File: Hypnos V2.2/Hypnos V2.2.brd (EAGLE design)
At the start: 25.6 x 52 mm, 32 parts

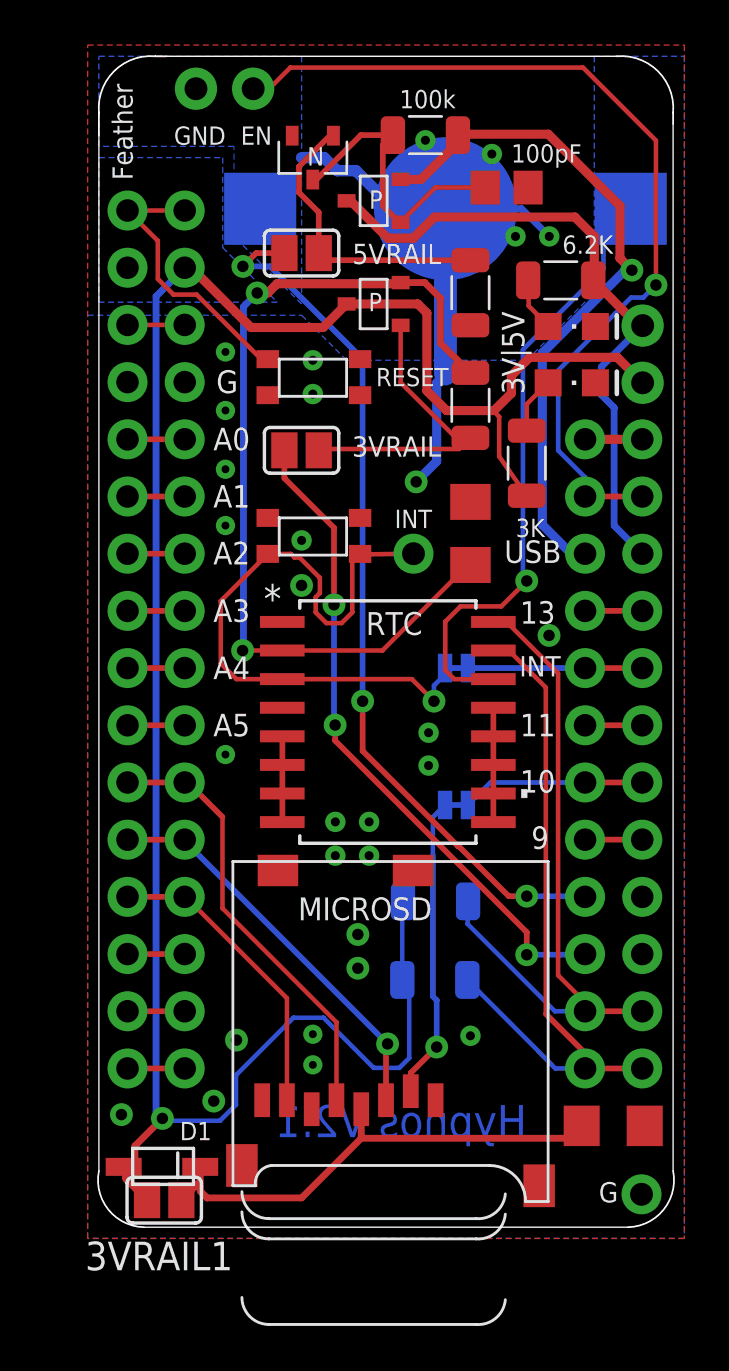
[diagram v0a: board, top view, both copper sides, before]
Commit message: Hypnos 2.2 and 3.2
+Change solder bridge to always connected pad
+Remove solder bridge for D1 diode
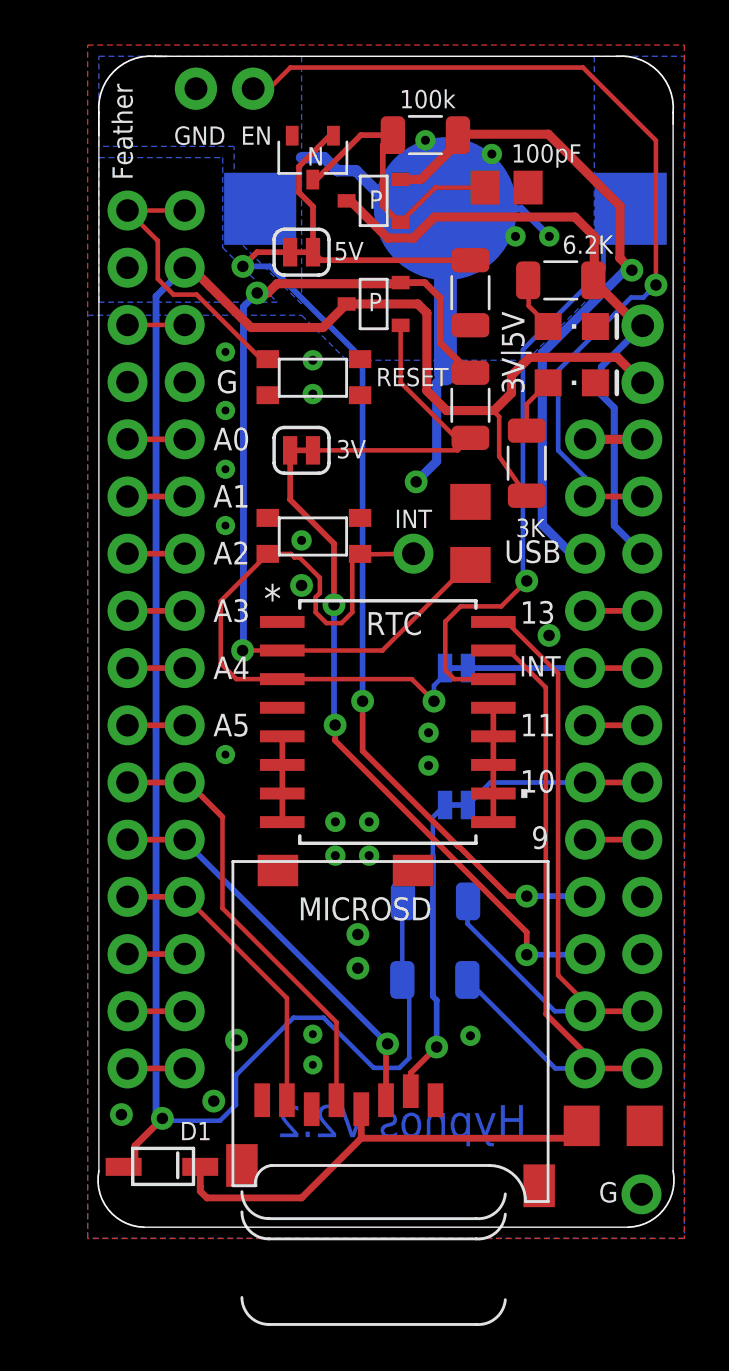
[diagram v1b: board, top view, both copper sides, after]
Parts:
- removed 3VRAIL, 3VRAIL1, 5VRAIL: (no value), jumper:SJ
- added 3V, 5V: (no value), SparkFun-Jumpers:SMT-JUMPER_2_NC_TRACE_SILK
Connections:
- removed net N$5: 3VRAIL.2, PMOS2.G, R2.1
- new net 5V: 3V.2, PMOS2.G, R2.1
- net 3VRAIL: no longer 3VRAIL1.2
- net N$1: now also 5V.1; no longer 5VRAIL.1
- net N$3: now also 3V.1; no longer 3VRAIL.1
- net N$4: now also 5V.2; no longer 5VRAIL.2
- net VDD: no longer 3VRAIL1.1
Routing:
- net 5V: track 0.00 -> 14.0 mm
- net N$5: track 13.8 -> 0.00 mm
- net 3VRAIL: track 97.2 -> 95.3 mm
- net VDD: track 22.0 -> 20.8 mm
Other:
- board text added: "Hypnos V2.2"
- board text removed: "Hypnos V2.1"
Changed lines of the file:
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@@
 <layer number="21" name="tPlace" color="7" fill="1" visible="yes" active="yes"/>
 <layer number="22" name="bPlace" color="7" fill="1" visible="yes" active="yes"/>
-<layer number="23" name="tOrigins" color="15" fill="1" visible="no" active="yes"/>
+<layer number="23" name="tOrigins" color="15" fill="1" visible="yes" active="yes"/>
 <layer number="24" name="bOrigins" color="15" fill="1" visible="yes" active="yes"/>
 <layer number="25" name="tNames" color="7" fill="1" visible="yes" active="yes"/>
@@
 <text x="12.18" y="17.66" size="1.016" layer="22" rot="MR270">Optional
 I2C Pull Up</text>
-<text x="20" y="4.5" size="1.4224" layer="16" ratio="15" rot="MR0">Hypnos V2.1</text>
+<text x="20" y="4.5" size="1.4224" layer="16" ratio="15" rot="MR0">Hypnos V2.2</text>
 <text x="18.2" y="2.9" size="1.016" layer="22" rot="MR0">OpenSlab</text>
 <text x="11.79" y="19.71" size="1.016" layer="22" ratio="10" rot="MR180">SDCS</text>
@@
 <text x="19.51" y="31.15" size="0.8128" layer="21">3K</text>
 <text x="23.2" y="1.6" size="0.9" layer="21" ratio="10">G</text>
-<text x="22.9" y="1.3" size="1.016" layer="22" rot="MR0">Bao Nguyen &amp; Bryson Goto</text>
+<text x="23.7" y="1.2" size="1.016" layer="22" rot="MR0">Bao Nguyen &amp; Bryson Goto</text>
 <wire x1="26.5" y1="50" x2="26.5" y2="49.5" width="0.0762" layer="20"/>
 <wire x1="1" y1="49" x2="1" y2="50" width="0.0762" layer="20"/>
@@
 <wire x1="2.5" y1="2.4" x2="2.5" y2="4" width="0.15" layer="21"/>
 <wire x1="4.5" y1="3.8" x2="4.5" y2="2.7" width="0.15" layer="21"/>
-<text x="20" y="4.5" size="1.4224" layer="30" ratio="15" rot="MR0">Hypnos V2.1</text>
+<text x="20" y="4.5" size="1.4224" layer="30" ratio="15" rot="MR0">Hypnos V2.2</text>
 </plain>
 <attributes>
@@
 <attribute name="VENDOR" value="Maxim Integrated Products" x="69.712" y="-7.546" size="1.778" layer="27" display="off"/>
 </element>
-<element name="5VRAIL" library="jumper" library_urn="urn:adsk.eagle:library:252" package="SJ" package3d_urn="urn:adsk.eagle:package:15471/1" value="" x="10" y="43.76" smashed="yes">
-<attribute name="NAME" x="12.259" y="43.273" size="0.9" layer="25" ratio="10"/>
-<attribute name="VALUE" x="10.4001" y="43.76" size="0.02" layer="27"/>
-</element>
-<element name="3VRAIL" library="jumper" library_urn="urn:adsk.eagle:library:252" package="SJ" package3d_urn="urn:adsk.eagle:package:15471/1" value="" x="10" y="35" smashed="yes">
-<attribute name="NAME" x="12.246" y="34.719" size="0.9" layer="25" ratio="10"/>
-<attribute name="VALUE" x="10.4001" y="35" size="0.02" layer="27"/>
-</element>
 <element name="R2" library="Resistor_Capacitor" library_urn="urn:adsk.eagle:library:11396451" package="RES_1206" package3d_urn="urn:adsk.eagle:package:10872898/2" value="30k" x="17.5" y="37" smashed="yes" rot="R90">
 <attribute name="CREATED_BY" value="PCBLayout.com" x="17.5" y="37" size="1.778" layer="27" rot="R90" display="off"/>
@@
 <attribute name="VALUE" x="5.705" y="6.355" size="1.27" layer="27" rot="R180"/>
 </element>
-<element name="3VRAIL1" library="jumper" library_urn="urn:adsk.eagle:library:252" package="SJ" package3d_urn="urn:adsk.eagle:package:15471/1" value="" x="3.9" y="1.7" smashed="yes" rot="R180">
-<attribute name="NAME" x="6.951" y="-0.143" size="1.27" layer="25" ratio="10" rot="R180"/>
-<attribute name="VALUE" x="3.4999" y="1.7" size="0.02" layer="27" rot="R180"/>
+<element name="5V" library="SparkFun-Jumpers" library_urn="urn:adsk.eagle:library:528" package="SMT-JUMPER_2_NC_TRACE_SILK" package3d_urn="urn:adsk.eagle:package:39281/1" value="" x="10" y="43.8" smashed="yes">
+<attribute name="NAME" x="12.1" y="43.443" size="0.8128" layer="25" font="vector" ratio="10" align="bottom-center"/>
+<attribute name="VALUE" x="10" y="42.657" size="0.6096" layer="27" font="vector" ratio="20" align="top-center"/>
+</element>
+<element name="3V" library="SparkFun-Jumpers" library_urn="urn:adsk.eagle:library:528" package="SMT-JUMPER_2_NC_TRACE_SILK" package3d_urn="urn:adsk.eagle:package:39281/1" value="" x="10" y="35" smashed="yes">
+<attribute name="NAME" x="12.2" y="34.643" size="0.8128" layer="25" font="vector" ratio="10" align="bottom-center"/>
+<attribute name="VALUE" x="10" y="33.857" size="0.6096" layer="27" font="vector" ratio="20" align="top-center"/>
 </element>
 </elements>
@@
 </signal>
 <signal name="N$1">
-<contactref element="5VRAIL" pad="1"/>
 <via x="7.3927125" y="43.1692" extent="1-16" drill="0.508"/>
 <wire x1="12.71" y1="39.0619125" x2="8.602646875" y2="43.169265625" width="0.254" layer="16"/>
@@
 <wire x1="12.71" y1="21.653025" x2="16.950925" y2="17.4121" width="0.254" layer="1"/>
 <wire x1="12.71" y1="23.86" x2="12.71" y2="21.653025" width="0.254" layer="1"/>
-<wire x1="9.238" y1="43.76" x2="7.9835125" y2="43.76" width="0.254" layer="1"/>
-<wire x1="7.3927125" y1="43.1692" x2="7.9835125" y2="43.76" width="0.254" layer="1"/>
 <contactref element="MS2" pad="20"/>
 <wire x1="20" y1="15.2" x2="22.56" y2="15.2" width="0.254" layer="16"/>
 <wire x1="22.56" y1="15.2" x2="22.59" y2="15.17" width="0.254" layer="16"/>
+<contactref element="5V" pad="1"/>
+<wire x1="9.492" y1="43.8" x2="8.0235125" y2="43.8" width="0.254" layer="1"/>
+<wire x1="8.0235125" y1="43.8" x2="7.3927125" y2="43.1692" width="0.254" layer="1"/>
 </signal>
 <signal name="N$3">
-<contactref element="3VRAIL" pad="1"/>
-<wire x1="11.44" y1="31.56" x2="9.238" y2="33.762" width="0.254" layer="1"/>
-<wire x1="9.238" y1="35" x2="9.238" y2="33.762" width="0.254" layer="1"/>
-<wire x1="11.44" y1="31.56" x2="11.44" y2="28.14" width="0.254" layer="1"/>
+<wire x1="11.44" y1="30.86" x2="11.44" y2="28.14" width="0.254" layer="1"/>
 <via x="11.44" y="28.14" extent="1-16" drill="0.508"/>
 <wire x1="11.44" y1="28.14" x2="11.44" y2="22.85" width="0.254" layer="16"/>
@@
 <wire x1="20" y1="12.6" x2="22.56" y2="12.6" width="0.254" layer="16"/>
 <wire x1="22.56" y1="12.6" x2="22.59" y2="12.63" width="0.254" layer="16"/>
+<contactref element="3V" pad="1"/>
+<wire x1="9.492" y1="35" x2="9.492" y2="32.808" width="0.254" layer="1"/>
+<wire x1="9.492" y1="32.808" x2="11.44" y2="30.86" width="0.254" layer="1"/>
 </signal>
 <signal name="5VUSB">
@@
 <wire x1="2.6" y1="3.4" x2="2.5" y2="3.3" width="0.3048" layer="1"/>
 <wire x1="2.5" y1="3.3" x2="2.1" y2="3.18" width="0.3048" layer="1"/>
-<contactref element="3VRAIL1" pad="2"/>
-<wire x1="3.138" y1="1.7" x2="2.2" y2="2.638" width="0.3048" layer="1"/>
-<wire x1="2.2" y1="2.638" x2="2.1" y2="3.18" width="0.3048" layer="1"/>
 <contactref element="R7" pad="1"/>
 <contactref element="R6" pad="1"/>
@@
 <wire x1="10.657625" y1="47.0255" x2="12.632125" y2="49" width="0.254" layer="1"/>
 </signal>
-<signal name="N$5">
-<contactref element="3VRAIL" pad="2"/>
+<signal name="5V">
 <contactref element="R2" pad="1"/>
 <contactref element="PMOS2" pad="G"/>
@@
 <wire x1="17.121728125" y1="35.288271875" x2="14.4" y2="38.01" width="0.2032" layer="1"/>
 <wire x1="14.4" y1="38.01" x2="14.4" y2="40.55" width="0.2032" layer="1"/>
-<wire x1="10.762" y1="35" x2="10.822" y2="35.06" width="0.2032" layer="1"/>
-<wire x1="16.9973625" y1="35.06" x2="17.474096875" y2="35.536734375" width="0.2032" layer="1"/>
-<wire x1="10.822" y1="35.06" x2="16.9973625" y2="35.06" width="0.2032" layer="1"/>
+<contactref element="3V" pad="2"/>
+<wire x1="16.9373625" y1="35" x2="17.474096875" y2="35.536734375" width="0.2032" layer="1"/>
+<wire x1="10.508" y1="35" x2="16.9373625" y2="35" width="0.2032" layer="1"/>
 </signal>
 <signal name="N$4">
-<contactref element="5VRAIL" pad="2"/>
 <contactref element="R1" pad="1"/>
 <contactref element="U$3" pad="1"/>
 <wire x1="9.8852" y1="46.448675" x2="9.8852" y2="47.602325" width="0.254" layer="1"/>
-<wire x1="9.8852" y1="46.448675" x2="10.762" y2="45.571875" width="0.254" layer="1"/>
 <wire x1="11.257375" y1="48.9745" x2="11.415" y2="48.9745" width="0.254" layer="1"/>
-<wire x1="11.257375" y1="48.9745" x2="9.8852" y2="47.602325" width="0.254" layer="1"/>
-<wire x1="17.5" y1="43.445" x2="11.077" y2="43.445" width="0.254" layer="1"/>
-<wire x1="11.077" y1="43.445" x2="11.011" y2="43.511" width="0.254" layer="1"/>
-<wire x1="10.762" y1="45.571875" x2="10.762" y2="43.76" width="0.254" layer="1"/>
-<wire x1="10.762" y1="43.76" x2="11.011" y2="43.511" width="0.254" layer="1"/>
+<wire x1="9.8852" y1="47.602325" x2="11.257375" y2="48.9745" width="0.254" layer="1"/>
+<contactref element="5V" pad="2"/>
+<wire x1="10.508" y1="45.825875" x2="9.8852" y2="46.448675" width="0.254" layer="1"/>
+<wire x1="10.508" y1="43.8" x2="10.508" y2="45.825875" width="0.254" layer="1"/>
+<wire x1="17.5" y1="43.445" x2="10.863" y2="43.445" width="0.254" layer="1"/>
+<wire x1="10.863" y1="43.445" x2="10.508" y2="43.8" width="0.254" layer="1"/>
 </signal>
 <signal name="N$11">
@@
 <wire x1="5.5" y1="2.3" x2="5.5" y2="3.08" width="0.3048" layer="1"/>
 <wire x1="5.5" y1="3.08" x2="5.5" y2="3.18" width="0.3048" layer="1"/>
-<contactref element="3VRAIL1" pad="1"/>
-<wire x1="5.381" y1="2.419" x2="4.662" y2="1.7" width="0.3048" layer="1"/>
-<wire x1="5.5" y1="2.3" x2="5.381" y2="2.419" width="0.3048" layer="1"/>
 </signal>
 </signals>
